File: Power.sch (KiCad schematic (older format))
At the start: 18 parts, among them P1 24 Pin MiniFit JR, SW1 Power Switch

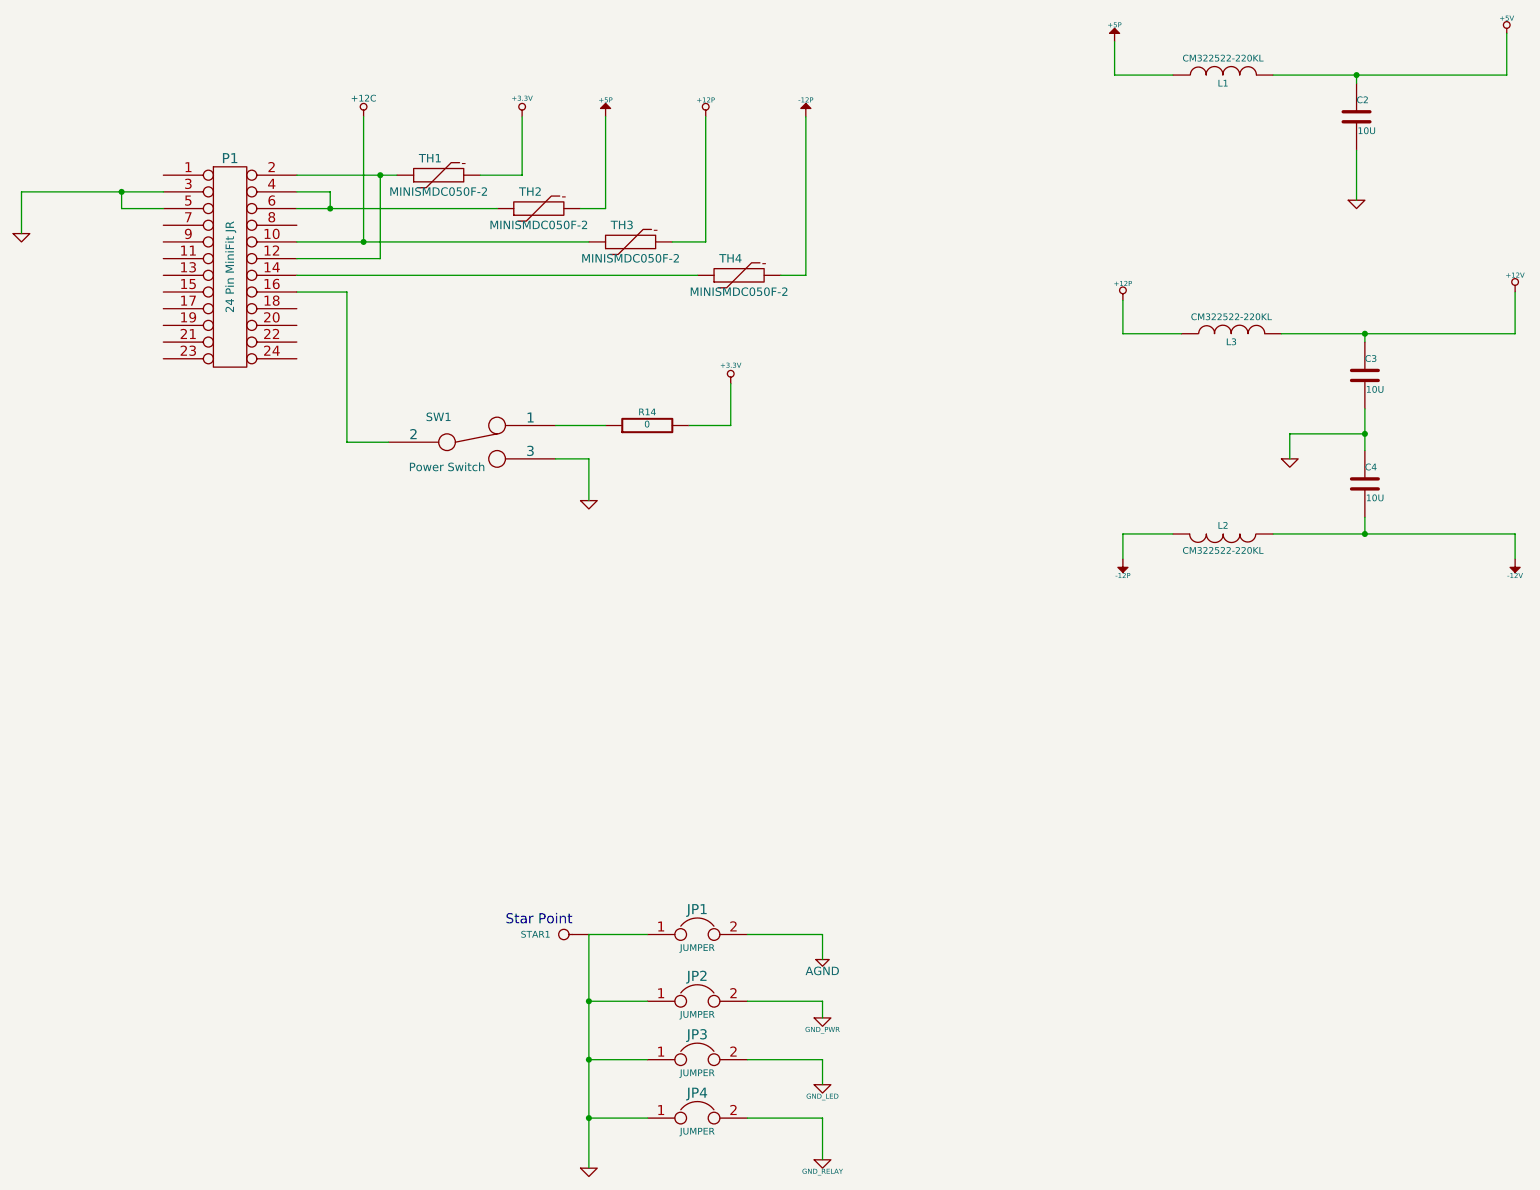
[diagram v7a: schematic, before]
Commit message: Added the schematic and BOM changes back in after hard reset
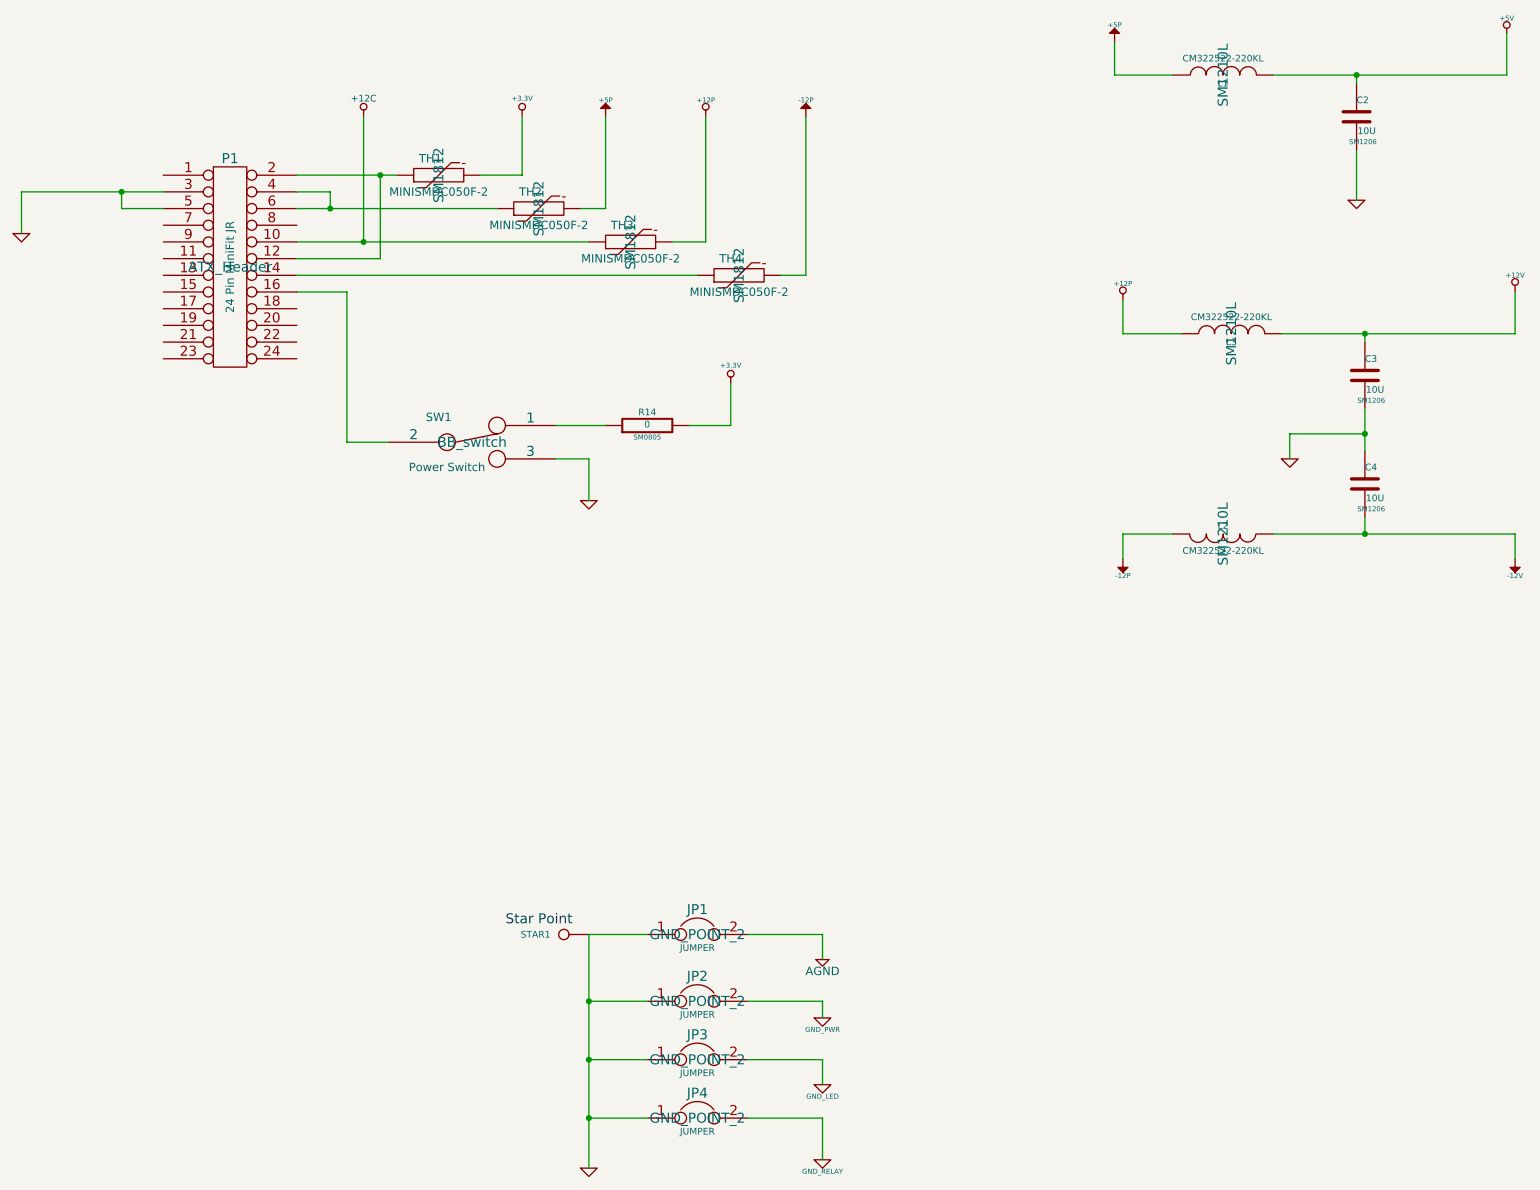
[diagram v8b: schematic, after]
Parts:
- C2, C3, C4: footprint ~ -> SM1206
- JP1, JP2, JP3, JP4: footprint ~ -> GND_POINT_2
- L1, L2, L3: footprint ~ -> SM1210L
- P1: footprint (none) -> ATX_Header
- R14: footprint ~ -> SM0805
- SW1: footprint ~ -> BB_switch
- TH1, TH2, TH3, TH4: footprint ~ -> SM1812
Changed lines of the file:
@@
-EESchema Schematic File Version 2  date 4/16/2014 11:04:06 PM
+EESchema Schematic File Version 2  date 4/18/2014 9:49:53 PM
 LIBS:power
 LIBS:device
@@
 Sheet 9 9
 Title ""
-Date "17 apr 2014"
+Date "19 apr 2014"
 Rev ""
 Comp ""
@@
 F 0 "P1" H 2650 2700 60  0000 C CNN
 F 1 "24 Pin MiniFit JR" V 2650 2050 50  0000 C CNN
-F 2 "" H 2650 2050 60  0000 C CNN
+F 2 "ATX_Header" H 2650 2050 60  0000 C CNN
 F 3 "" H 2650 2050 60  0000 C CNN
 F 4 "Molex" H 2650 2050 60  0001 C CNN "MFG Name"
@@
 F 0 "SW1" H 3900 3250 50  0000 C CNN
 F 1 "Power Switch" H 3950 2950 50  0000 C CNN
-F 2 "~" H 4100 3100 60  0000 C CNN
+F 2 "BB_switch" H 4100 3100 60  0000 C CNN
 F 3 "~" H 4100 3100 60  0000 C CNN
 F 4 "C&K Components" H 4100 3100 60  0001 C CNN "MFG Name"
@@
 F 0 "R14" V 5230 3000 40  0000 C CNN
 F 1 "0" V 5157 3001 40  0000 C CNN
-F 2 "~" V 5080 3000 30  0000 C CNN
+F 2 "SM0805" V 5080 3000 30  0000 C CNN
 F 3 "~" H 5150 3000 30  0000 C CNN
 	1    5150 3000
@@
 F 0 "C3" H 9450 2800 40  0000 L CNN
 F 1 "10U" H 9456 2615 40  0000 L CNN
-F 2 "~" H 9488 2550 30  0000 C CNN
+F 2 "SM1206" H 9488 2550 30  0000 C CNN
 F 3 "~" H 9450 2700 60  0000 C CNN
 	1    9450 2700
@@
 F 0 "C4" H 9450 3450 40  0000 L CNN
 F 1 "10U" H 9456 3265 40  0000 L CNN
-F 2 "~" H 9488 3200 30  0000 C CNN
+F 2 "SM1206" H 9488 3200 30  0000 C CNN
 F 3 "~" H 9450 3350 60  0000 C CNN
 	1    9450 3350
@@
 F 0 "TH1" V 4000 1550 50  0000 C CNN
 F 1 "MINISMDC050F-2" V 3800 1500 50  0000 C CNN
-F 2 "~" H 3900 1500 60  0000 C CNN
+F 2 "SM1812" H 3900 1500 60  0000 C CNN
 F 3 "~" H 3900 1500 60  0000 C CNN
 F 4 "TE Connectivity" H 3900 1500 60  0001 C CNN "MFG Name"
@@
 F 0 "L1" V 8550 900 40  0000 C CNN
 F 1 "CM322522-220KL" V 8700 900 40  0000 C CNN
-F 2 "~" H 8600 900 60  0000 C CNN
+F 2 "SM1210L" H 8600 900 60  0000 C CNN
 F 3 "~" H 8600 900 60  0000 C CNN
 F 4 "Bournes" H 8600 900 60  0001 C CNN "MFG Name"
@@
 F 0 "C2" H 9400 1250 40  0000 L CNN
 F 1 "10U" H 9406 1065 40  0000 L CNN
-F 2 "~" H 9438 1000 30  0000 C CNN
+F 2 "SM1206" H 9438 1000 30  0000 C CNN
 F 3 "~" H 9400 1150 60  0000 C CNN
 	1    9400 1150
@@
 F 0 "TH2" V 4600 1750 50  0000 C CNN
 F 1 "MINISMDC050F-2" V 4400 1700 50  0000 C CNN
-F 2 "~" H 4500 1700 60  0000 C CNN
+F 2 "SM1812" H 4500 1700 60  0000 C CNN
 F 3 "~" H 4500 1700 60  0000 C CNN
 F 4 "TE Connectivity" H 4500 1700 60  0001 C CNN "MFG Name"
@@
 F 0 "TH3" V 5150 1950 50  0000 C CNN
 F 1 "MINISMDC050F-2" V 4950 1900 50  0000 C CNN
-F 2 "~" H 5050 1900 60  0000 C CNN
+F 2 "SM1812" H 5050 1900 60  0000 C CNN
 F 3 "~" H 5050 1900 60  0000 C CNN
 F 4 "TE Connectivity" H 5050 1900 60  0001 C CNN "MFG Name"
@@
 F 0 "TH4" V 5800 2150 50  0000 C CNN
 F 1 "MINISMDC050F-2" V 5600 2100 50  0000 C CNN
-F 2 "~" H 5700 2100 60  0000 C CNN
+F 2 "SM1812" H 5700 2100 60  0000 C CNN
 F 3 "~" H 5700 2100 60  0000 C CNN
 F 4 "TE Connectivity" H 5700 2100 60  0001 C CNN "MFG Name"
@@
 F 0 "L3" V 8600 2450 40  0000 C CNN
 F 1 "CM322522-220KL" V 8750 2450 40  0000 C CNN
-F 2 "~" H 8650 2450 60  0000 C CNN
+F 2 "SM1210L" H 8650 2450 60  0000 C CNN
 F 3 "~" H 8650 2450 60  0000 C CNN
 F 4 "Bournes" H 8650 2450 60  0001 C CNN "MFG Name"
@@
 F 0 "L2" V 8550 3650 40  0000 C CNN
 F 1 "CM322522-220KL" V 8700 3650 40  0000 C CNN
-F 2 "~" H 8600 3650 60  0000 C CNN
+F 2 "SM1210L" H 8600 3650 60  0000 C CNN
 F 3 "~" H 8600 3650 60  0000 C CNN
 F 4 "Bournes" H 8600 3650 60  0001 C CNN "MFG Name"
@@
 F 0 "JP1" H 5450 6200 60  0000 C CNN
 F 1 "JUMPER" H 5450 5970 40  0000 C CNN
-F 2 "~" H 5450 6050 60  0000 C CNN
+F 2 "GND_POINT_2" H 5450 6050 60  0000 C CNN
 F 3 "~" H 5450 6050 60  0000 C CNN
 	1    5450 6050
@@
 F 0 "JP2" H 5450 6600 60  0000 C CNN
 F 1 "JUMPER" H 5450 6370 40  0000 C CNN
-F 2 "~" H 5450 6450 60  0000 C CNN
+F 2 "GND_POINT_2" H 5450 6450 60  0000 C CNN
 F 3 "~" H 5450 6450 60  0000 C CNN
 	1    5450 6450
@@
 F 0 "JP3" H 5450 6950 60  0000 C CNN
 F 1 "JUMPER" H 5450 6720 40  0000 C CNN
-F 2 "~" H 5450 6800 60  0000 C CNN
+F 2 "GND_POINT_2" H 5450 6800 60  0000 C CNN
 F 3 "~" H 5450 6800 60  0000 C CNN
 	1    5450 6800
@@
 F 0 "JP4" H 5450 7300 60  0000 C CNN
 F 1 "JUMPER" H 5450 7070 40  0000 C CNN
-F 2 "~" H 5450 7150 60  0000 C CNN
+F 2 "GND_POINT_2" H 5450 7150 60  0000 C CNN
 F 3 "~" H 5450 7150 60  0000 C CNN
 	1    5450 7150
